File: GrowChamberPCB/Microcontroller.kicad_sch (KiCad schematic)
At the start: 5 parts, among them U1 ESP32-S3-WROOM-1U

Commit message: some USB stuff
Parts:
- added C15, C16: DNP, symbol Device:C
- added R7, R8: 22pF, symbol Device:R
- added U3: USBLC6-2SC6, Package_TO_SOT_SMD:SOT-23-6, symbol Power_Protection:USBLC6-2SC6
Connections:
- net GND: now also C15.2, C16.2, U3.2 (GND)
- net at U1.13 (IO19): now also R7.1
- net at U1.14 (IO20): now also R8.1
- new net: C15.1, R8.2, U3.1 (I/O1)
- new net: C16.1, R7.2, U3.3 (I/O2)
- new net D+: U3.6 (I/O1)
- new net D-: U3.4 (I/O2)
- new net VBUS: U3.5 (VBUS)

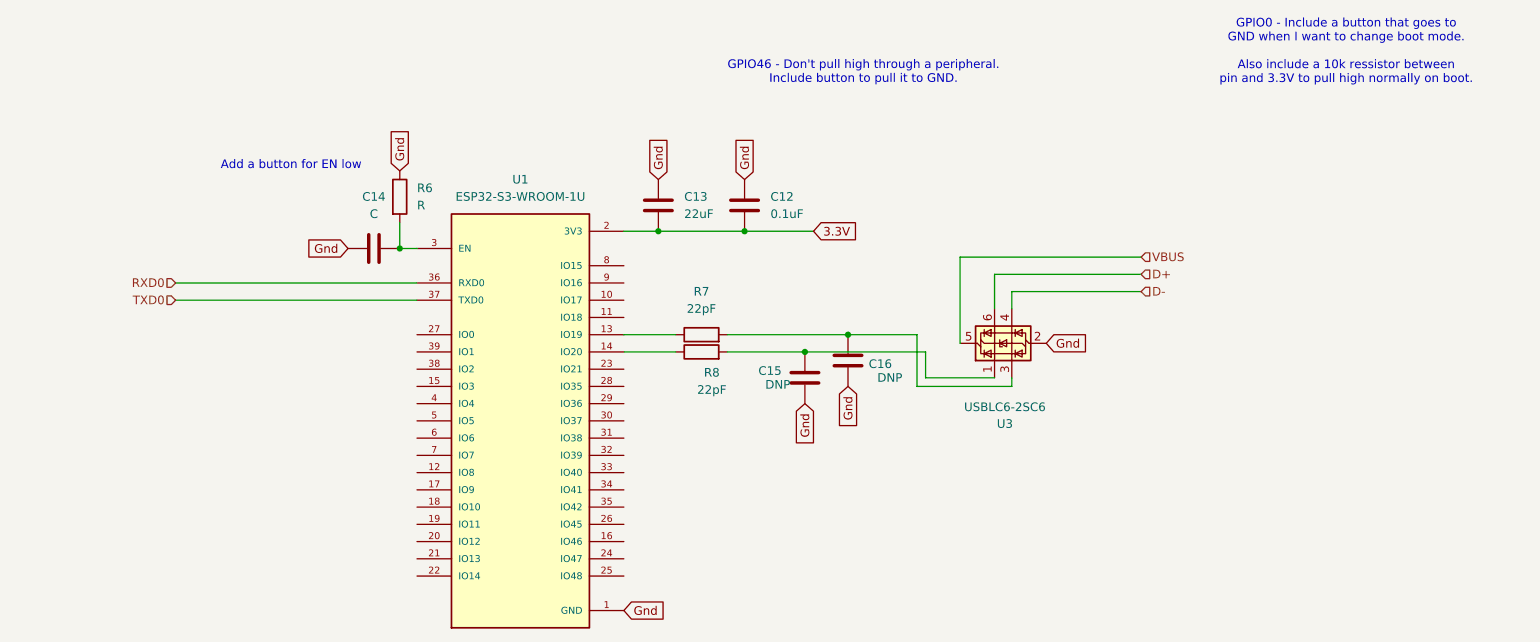
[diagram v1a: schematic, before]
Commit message: USB and buttons added to schematic
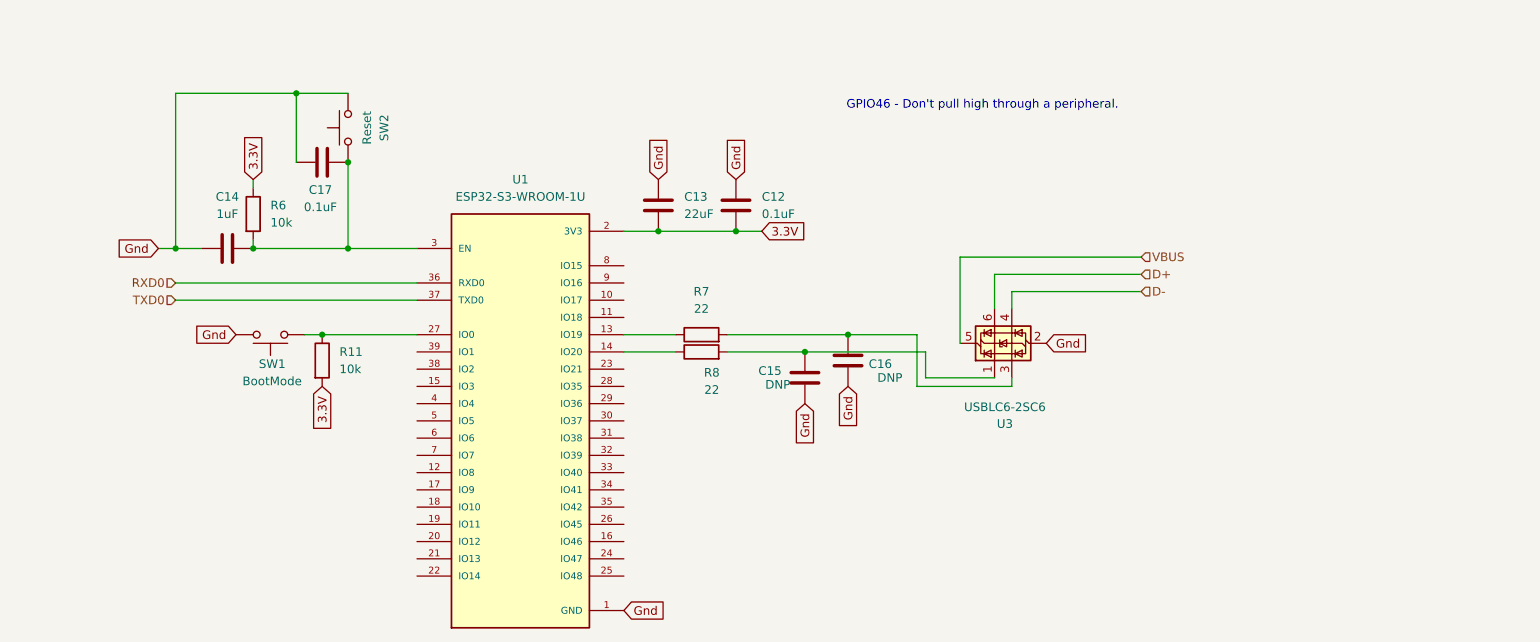
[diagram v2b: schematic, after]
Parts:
- added C17: 0.1uF, symbol Device:C
- added R11: 10k, symbol Device:R
- added SW1: BootMode, symbol Switch:SW_Push
- added SW2: Reset, symbol Switch:SW_Push
- C14: value C -> 1uF
- R6: value R -> 10k
- R7, R8: value 22pF -> 22
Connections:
- net 3.3V: now also R6.1, R11.2
- net GND: now also C17.1, SW1.2, SW2.2; no longer R6.1
- net at U1.27 (IO0): now also R11.1, SW1.1
- net at C14.2, R6.2, U1.3 (EN): now also C17.2, SW2.1
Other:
- note added: "GPIO46 - Don't pull high through a peripheral."
- note removed: "Add a button for EN low"
- note removed: "GPIO0 - Include a button that goes to GND when I want to change boot mode. Also include a 10k ressistor between pin and 3.3V to pull high normally on boot."
- note removed: "GPIO46 - Don't pull high through a peripheral. Include button to pull it to GND."
- moved on the sheet: C12, C14, R6

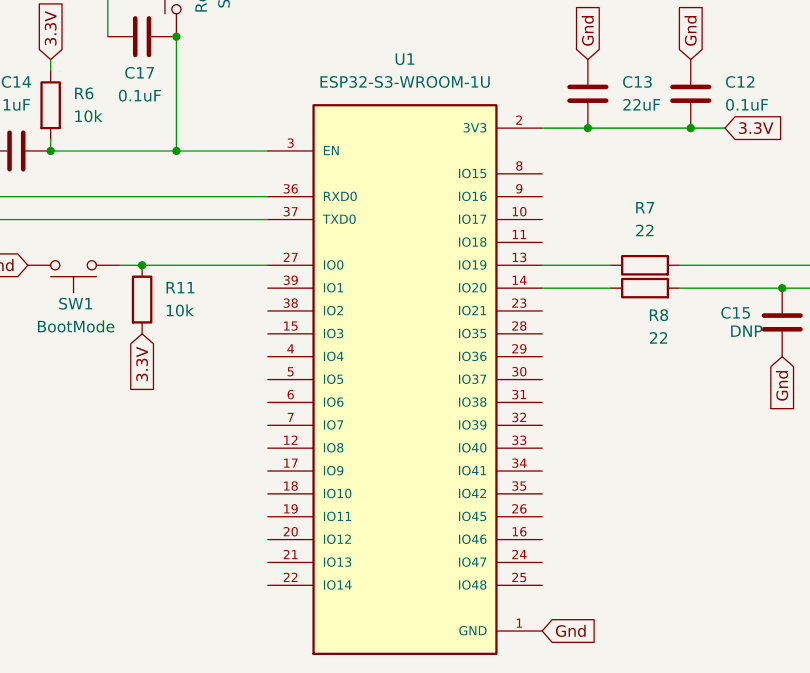
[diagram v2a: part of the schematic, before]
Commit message: GPIO labeling and mist maker added
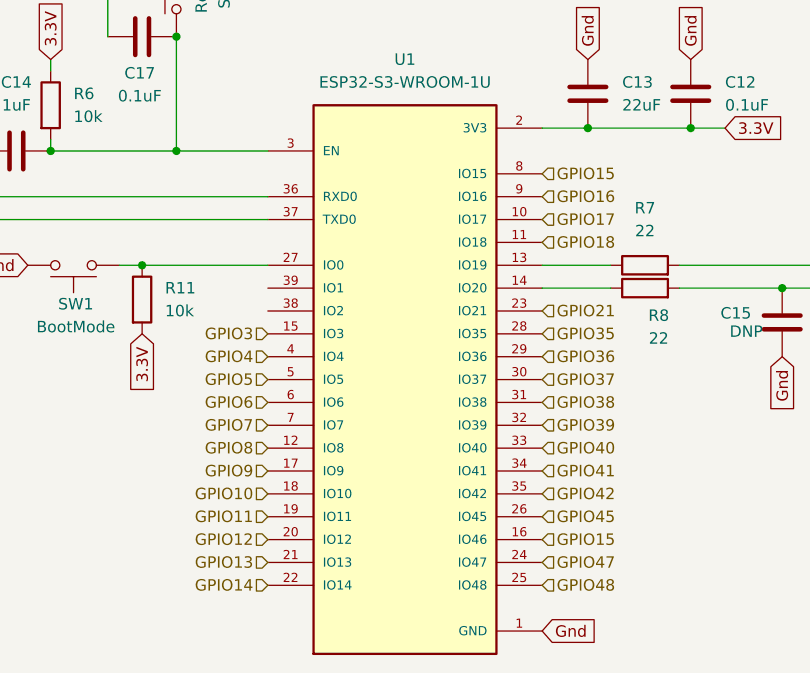
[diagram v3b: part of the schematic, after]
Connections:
- net GPIO17: now reaches U1.10 (IO17)
- net GPIO18: now reaches U1.11 (IO18)
- net GPIO8: now reaches U1.12 (IO8)
- net GPIO3: now reaches U1.15 (IO3)
- net GPIO15: now reaches U1.16 (IO46)
- net GPIO15: now also U1.8 (IO15)
- net GPIO9: now reaches U1.17 (IO9)
- net GPIO10: now reaches U1.18 (IO10)
- net GPIO11: now reaches U1.19 (IO11)
- net GPIO12: now reaches U1.20 (IO12)
- net GPIO13: now reaches U1.21 (IO13)
- net GPIO14: now reaches U1.22 (IO14)
- net GPIO21: now reaches U1.23 (IO21)
- net GPIO47: now reaches U1.24 (IO47)
- net GPIO48: now reaches U1.25 (IO48)
- net GPIO45: now reaches U1.26 (IO45)
- net GPIO35: now reaches U1.28 (IO35)
- net GPIO36: now reaches U1.29 (IO36)
- net GPIO37: now reaches U1.30 (IO37)
- net GPIO38: now reaches U1.31 (IO38)
- net GPIO39: now reaches U1.32 (IO39)
- net GPIO40: now reaches U1.33 (IO40)
- net GPIO41: now reaches U1.34 (IO41)
- net GPIO42: now reaches U1.35 (IO42)
- net GPIO4: now reaches U1.4 (IO4)
- net GPIO5: now reaches U1.5 (IO5)
- net GPIO6: now reaches U1.6 (IO6)
- net GPIO7: now reaches U1.7 (IO7)
- net GPIO16: now reaches U1.9 (IO16)

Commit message: stuff
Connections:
- net GPIO4 renamed CS_Memory / GPIO4
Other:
- moved on the sheet: R11, SW1
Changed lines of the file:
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@@
+	)
+	(junction
+		(at 82.55 64.77)
+		(diameter 0)
+		(color 0 0 0 0)
 	)
 	(junction
@@
 	)
 	(junction
-		(at 104.14 66.04)
-		(diameter 0)
-		(color 0 0 0 0)
-	)
-	(junction
 		(at 100.33 30.48)
 		(diameter 0)
@@
 	)
 	(junction
+		(at 86.36 66.04)
+		(diameter 0)
+		(color 0 0 0 0)
+	)
+	(junction
+		(at 78.74 64.77)
+		(diameter 0)
+		(color 0 0 0 0)
+	)
+	(junction
 		(at 181.61 66.04)
 		(diameter 0)
@@
 	(wire
 		(pts
+			(xy 78.74 64.77) (xy 82.55 64.77)
+		)
+		(stroke
+			(width 0)
+			(type default)
+		)
+	)
+	(wire
+		(pts
 			(xy 82.55 30.48) (xy 100.33 30.48)
 		)
@@
 	(wire
 		(pts
+			(xy 86.36 64.77) (xy 86.36 66.04)
+		)
+		(stroke
+			(width 0)
+			(type default)
+		)
+	)
+	(wire
+		(pts
 			(xy 193.04 72.39) (xy 193.04 68.58)
 		)
@@
 	(wire
 		(pts
-			(xy 101.6 66.04) (xy 104.14 66.04)
+			(xy 86.36 66.04) (xy 118.11 66.04)
+		)
+		(stroke
+			(width 0)
+			(type default)
+		)
+	)
+	(wire
+		(pts
+			(xy 76.2 64.77) (xy 78.74 64.77)
 		)
 		(stroke
@@
 	(wire
 		(pts
+			(xy 82.55 64.77) (xy 86.36 64.77)
+		)
+		(stroke
+			(width 0)
+			(type default)
+		)
+	)
+	(wire
+		(pts
 			(xy 107.95 53.34) (xy 118.11 53.34)
 		)
@@
 	(wire
 		(pts
+			(xy 82.55 64.77) (xy 82.55 66.04)
+		)
+		(stroke
+			(width 0)
+			(type default)
+		)
+	)
+	(wire
+		(pts
 			(xy 153.67 50.8) (xy 165.1 50.8)
 		)
@@
 	(wire
 		(pts
-			(xy 118.11 66.04) (xy 104.14 66.04)
-		)
-		(stroke
-			(width 0)
-			(type default)
-		)
-	)
-	(wire
-		(pts
 			(xy 100.33 30.48) (xy 107.95 30.48)
+		)
+		(stroke
+			(width 0)
+			(type default)
+		)
+	)
+	(wire
+		(pts
+			(xy 82.55 66.04) (xy 86.36 66.04)
 		)
 		(stroke
@@
 		)
 	)
+	(global_label "CS_Memory {slash} GPIO4"
+		(shape input)
+		(at 118.11 76.2 180)
+		(fields_autoplaced yes)
+		(effects
+			(font
+				(size 1.27 1.27)
+			)
+			(justify right)
+		)
+		(property "Intersheetrefs" "${INTERSHEET_REFS}"
+			(at 95.5911 76.2 0)
+			(effects
+				(font
+					(size 1.27 1.27)
+				)
+				(justify right)
+				(hide yes)
+			)
+		)
+	)
 	(global_label "Gnd"
 		(shape input)
-		(at 91.44 66.04 180)
+		(at 66.04 64.77 180)
 		(fields_autoplaced yes)
 		(effects
@@
 		)
 		(property "Intersheetrefs" "${INTERSHEET_REFS}"
-			(at 84.8868 66.04 0)
+			(at 59.4868 64.77 0)
 			(effects
 				(font
@@
 	(global_label "3.3V"
 		(shape input)
-		(at 104.14 73.66 270)
+		(at 78.74 72.39 270)
 		(fields_autoplaced yes)
 		(effects
@@
 		)
 		(property "Intersheetrefs" "${INTERSHEET_REFS}"
-			(at 104.14 80.7576 90)
+			(at 78.74 79.4876 90)
 			(effects
 				(font
@@
 		)
 	)
-	(hierarchical_label "GPIO4"
-		(shape input)
-		(at 118.11 76.2 180)
+	(hierarchical_label "GPIO9"
+		(shape input)
+		(at 118.11 88.9 180)
 		(effects
 			(font
@@
 		)
 	)
-	(hierarchical_label "GPIO9"
-		(shape input)
-		(at 118.11 88.9 180)
+	(hierarchical_label "GPIO15"
+		(shape input)
+		(at 148.59 96.52 0)
+		(effects
+			(font
+				(size 1.27 1.27)
+			)
+			(justify left)
+		)
+	)
+	(hierarchical_label "GPIO8"
+		(shape input)
+		(at 118.11 86.36 180)
 		(effects
 			(font
@@
 		)
 	)
-	(hierarchical_label "GPIO15"
-		(shape input)
-		(at 148.59 96.52 0)
+	(hierarchical_label "GPIO45"
+		(shape input)
+		(at 148.59 93.98 0)
 		(effects
 			(font
@@
 			)
 			(justify right)
-		)
-	)
-	(hierarchical_label "GPIO8"
-		(shape input)
-		(at 118.11 86.36 180)
-		(effects
-			(font
-				(size 1.27 1.27)
-			)
-			(justify right)
-		)
-	)
-	(hierarchical_label "GPIO45"
-		(shape input)
-		(at 148.59 93.98 0)
-		(effects
-			(font
-				(size 1.27 1.27)
-			)
-			(justify left)
 		)
 	)
@@
 		)
 		(instances
-			(project ""
+			(project "GrowChamberPCB"
 				(path "/39371779-5336-4073-adec-fb32caf6a86f/10f1dbf8-4cce-44c0-b6de-eccec8d65f6f"
 					(reference "U1")
@@
 		)
 		(instances
-			(project ""
+			(project "GrowChamberPCB"
 				(path "/39371779-5336-4073-adec-fb32caf6a86f/10f1dbf8-4cce-44c0-b6de-eccec8d65f6f"
 					(reference "R6")
@@
 		)
 		(instances
-			(project ""
+			(project "GrowChamberPCB"
 				(path "/39371779-5336-4073-adec-fb32caf6a86f/10f1dbf8-4cce-44c0-b6de-eccec8d65f6f"
 					(reference "C13")
@@
 		)
 		(instances
-			(project ""
+			(project "GrowChamberPCB"
 				(path "/39371779-5336-4073-adec-fb32caf6a86f/10f1dbf8-4cce-44c0-b6de-eccec8d65f6f"
 					(reference "R8")
@@
 		)
 		(instances
-			(project ""
+			(project "GrowChamberPCB"
 				(path "/39371779-5336-4073-adec-fb32caf6a86f/10f1dbf8-4cce-44c0-b6de-eccec8d65f6f"
 					(reference "C14")
@@
 		)
 		(instances
-			(project ""
+			(project "GrowChamberPCB"
 				(path "/39371779-5336-4073-adec-fb32caf6a86f/10f1dbf8-4cce-44c0-b6de-eccec8d65f6f"
 					(reference "C16")
@@
 		)
 		(instances
-			(project ""
+			(project "GrowChamberPCB"
 				(path "/39371779-5336-4073-adec-fb32caf6a86f/10f1dbf8-4cce-44c0-b6de-eccec8d65f6f"
 					(reference "U3")
@@
 		)
 		(instances
-			(project ""
+			(project "GrowChamberPCB"
 				(path "/39371779-5336-4073-adec-fb32caf6a86f/10f1dbf8-4cce-44c0-b6de-eccec8d65f6f"
 					(reference "R7")
@@
 		)
 		(instances
-			(project ""
+			(project "GrowChamberPCB"
 				(path "/39371779-5336-4073-adec-fb32caf6a86f/10f1dbf8-4cce-44c0-b6de-eccec8d65f6f"
 					(reference "C12")
@@
 	(symbol
 		(lib_id "Device:R")
-		(at 104.14 69.85 0)
+		(at 78.74 68.58 0)
 		(unit 1)
 		(exclude_from_sim no)
@@
 		(fields_autoplaced yes)
 		(property "Reference" "R11"
-			(at 106.68 68.5799 0)
+			(at 81.28 67.3099 0)
 			(effects
 				(font
@@
 		)
 		(property "Value" "10k"
-			(at 106.68 71.1199 0)
+			(at 81.28 69.8499 0)
 			(effects
 				(font
@@
 		)
 		(property "Footprint" ""
-			(at 102.362 69.85 90)
+			(at 76.962 68.58 90)
 			(effects
 				(font
@@
 		)
 		(property "Datasheet" "~"
-			(at 104.14 69.85 0)
+			(at 78.74 68.58 0)
 			(effects
 				(font
@@
 		)
 		(property "Description" "Resistor"
-			(at 104.14 69.85 0)
+			(at 78.74 68.58 0)
 			(effects
 				(font
@@
 		)
 		(instances
-			(project ""
+			(project "GrowChamberPCB"
 				(path "/39371779-5336-4073-adec-fb32caf6a86f/10f1dbf8-4cce-44c0-b6de-eccec8d65f6f"
 					(reference "R11")
@@
 		)
 		(instances
-			(project ""
+			(project "GrowChamberPCB"
 				(path "/39371779-5336-4073-adec-fb32caf6a86f/10f1dbf8-4cce-44c0-b6de-eccec8d65f6f"
 					(reference "C15")
@@
 	(symbol
 		(lib_id "Switch:SW_Push")
-		(at 96.52 66.04 180)
+		(at 71.12 64.77 180)
 		(unit 1)
 		(exclude_from_sim no)
@@
 		(dnp no)
 		(property "Reference" "SW1"
-			(at 96.774 70.358 0)
+			(at 71.374 69.088 0)
 			(effects
 				(font
@@
 		)
 		(property "Value" "BootMode"
-			(at 96.774 72.898 0)
+			(at 71.374 71.628 0)
 			(effects
 				(font
@@
 		)
 		(property "Footprint" ""
-			(at 96.52 71.12 0)
+			(at 71.12 69.85 0)
 			(effects
 				(font
@@
 		)
 		(property "Datasheet" "~"
-			(at 96.52 71.12 0)
+			(at 71.12 69.85 0)
 			(effects
 				(font
@@
 		)
 		(property "Description" "Push button switch, generic, two pins"
-			(at 96.52 66.04 0)
+			(at 71.12 64.77 0)
 			(effects
 				(font
@@
 		)
 		(instances
-			(project ""
+			(project "GrowChamberPCB"
 				(path "/39371779-5336-4073-adec-fb32caf6a86f/10f1dbf8-4cce-44c0-b6de-eccec8d65f6f"
 					(reference "SW1")

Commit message: bunch o stuff
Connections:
- net GPIO15: no longer U1.16 (IO46)
- net CS_Memory / GPIO4 renamed GPIO4
- net GPIO21 renamed CS_SD
- net GPIO3 renamed SD_Detect
- net GPIO38 renamed CS_Display
- net GPIO39 renamed DC_Display
- net GPIO40 renamed SCK
- net GPIO41 renamed MOSI
- net GPIO42 renamed MISO
- net GPIO47 renamed Display_Reset
- net GPIO48 renamed CS_Memory
- new net GPIO46: U1.16 (IO46)
